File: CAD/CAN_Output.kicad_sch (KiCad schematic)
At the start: 10 parts, among them U4 MCP251863T-E/9PX, Y2 Crystal_GND24

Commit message: updated baord
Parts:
- C18, C19: value 11.5p -> 18p
- Y2: value Crystal_GND24 -> 40MHz
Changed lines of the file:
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@@
 	(label "OSC1"
 		(at 45.72 146.05 0)
-		(fields_autoplaced yes)
 		(effects
 			(font
@@
 	(label "OSC1"
 		(at 78.74 85.09 0)
-		(fields_autoplaced yes)
 		(effects
 			(font
@@
 	(label "OSC2"
 		(at 60.96 146.05 0)
-		(fields_autoplaced yes)
 		(effects
 			(font
@@
 	(label "OSC2"
 		(at 78.74 82.55 0)
-		(fields_autoplaced yes)
 		(effects
 			(font
@@
 		(shape output)
 		(at 154.94 85.09 0)
-		(fields_autoplaced yes)
 		(effects
 			(font
@@
 		(shape output)
 		(at 158.75 107.95 0)
-		(fields_autoplaced yes)
 		(effects
 			(font
@@
 		(shape input)
 		(at 154.94 87.63 0)
-		(fields_autoplaced yes)
 		(effects
 			(font
@@
 		(shape output)
 		(at 154.94 92.71 0)
-		(fields_autoplaced yes)
 		(effects
 			(font
@@
 		(shape output)
 		(at 78.74 92.71 180)
-		(fields_autoplaced yes)
 		(effects
 			(font
@@
 		(shape output)
 		(at 154.94 90.17 0)
-		(fields_autoplaced yes)
 		(effects
 			(font
@@
 		(shape output)
 		(at 78.74 80.01 180)
-		(fields_autoplaced yes)
 		(effects
 			(font
@@
 		(shape output)
 		(at 170.18 105.41 0)
-		(fields_autoplaced yes)
 		(effects
 			(font
@@
 			)
 		)
-		(property "Value" "11.5p"
+		(property "Value" "18p"
 			(at 41.91 151.1299 0)
 			(effects
@@
 			)
 		)
-		(property "Value" "11.5p"
+		(property "Value" "18p"
 			(at 66.04 151.1299 0)
 			(effects
@@
 			)
 		)
-		(property "Value" "Crystal_GND24"
+		(property "Value" "40MHz"
 			(at 67.31 142.2714 0)
 			(effects
@@
 			)
 		)
-		(property "Datasheet" "~"
+		(property "Datasheet" "ABM8G-40.000MHZ-18-D2Y-T"
 			(at 55.88 146.05 0)
 			(effects

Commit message: updated board
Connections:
- net GND: now also U4.29 (EP)
- net nINT1: now also U4.9 (nINT0/GPIO0/XSTBY); no longer U4.8 (nINT1/GPIO1)
- no-connect marks 4 -> 3
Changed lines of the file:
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@@
 	)
 	(no_connect
-		(at 154.94 74.93)
-	)
-	(no_connect
-		(at 83.82 95.25)
+		(at 83.82 92.71)
 	)
 	(no_connect
@@
 	(wire
 		(pts
+			(xy 154.94 74.93) (xy 166.37 74.93)
+		)
+		(stroke
+			(width 0)
+			(type default)
+		)
+	)
+	(wire
+		(pts
 			(xy 82.55 97.79) (xy 82.55 90.17)
 		)
@@
 	(wire
 		(pts
+			(xy 80.01 92.71) (xy 78.74 92.71)
+		)
+		(stroke
+			(width 0)
+			(type default)
+		)
+	)
+	(wire
+		(pts
 			(xy 83.82 97.79) (xy 82.55 97.79)
 		)
@@
 	(wire
 		(pts
-			(xy 78.74 92.71) (xy 83.82 92.71)
-		)
-		(stroke
-			(width 0)
-			(type default)
-		)
-	)
-	(wire
-		(pts
 			(xy 161.29 97.79) (xy 161.29 77.47)
 		)
@@
 	(wire
 		(pts
+			(xy 83.82 95.25) (xy 80.01 95.25)
+		)
+		(stroke
+			(width 0)
+			(type default)
+		)
+	)
+	(wire
+		(pts
 			(xy 78.74 85.09) (xy 83.82 85.09)
 		)
@@
 		(pts
 			(xy 71.12 115.57) (xy 82.55 115.57)
+		)
+		(stroke
+			(width 0)
+			(type default)
+		)
+	)
+	(wire
+		(pts
+			(xy 80.01 95.25) (xy 80.01 92.71)
 		)
 		(stroke
@@
 		)
 	)
+	(symbol
+		(lib_id "power:GND")
+		(at 166.37 74.93 0)
+		(unit 1)
+		(exclude_from_sim no)
+		(in_bom yes)
+		(on_board yes)
+		(dnp no)
+		(fields_autoplaced yes)
+		(property "Reference" "#PWR039"
+			(at 166.37 81.28 0)
+			(effects
+				(font
+					(size 1.27 1.27)
+				)
+				(hide yes)
+			)
+		)
+		(property "Value" "GND"
+			(at 166.37 80.01 0)
+			(effects
+				(font
+					(size 1.27 1.27)
+				)
+			)
+		)
+		(property "Footprint" ""
+			(at 166.37 74.93 0)
+			(effects
+				(font
+					(size 1.27 1.27)
+				)
+				(hide yes)
+			)
+		)
+		(property "Datasheet" ""
+			(at 166.37 74.93 0)
+			(effects
+				(font
+					(size 1.27 1.27)
+				)
+				(hide yes)
+			)
+		)
+		(property "Description" "Power symbol creates a global label with name \"GND\" , ground"
+			(at 166.37 74.93 0)
+			(effects
+				(font
+					(size 1.27 1.27)
+				)
+				(hide yes)
+			)
+		)
+		(pin "1"
+		)
+		(instances
+			(project ""
+				(path "/7d82ce85-7222-412b-9514-e26c0dea1256/32242d8d-0269-4405-8d3b-a17d7bfa44f1"
+					(reference "#PWR039")
+					(unit 1)
+				)
+				(path "/7d82ce85-7222-412b-9514-e26c0dea1256/3a8c1e9a-a729-42c6-9176-105dc8f8e86f"
+					(reference "#PWR071")
+					(unit 1)
+				)
+				(path "/7d82ce85-7222-412b-9514-e26c0dea1256/74c494bc-ee2a-4fe5-bc69-1ba1e57f619f"
+					(reference "#PWR056")
+					(unit 1)
+				)
+				(path "/7d82ce85-7222-412b-9514-e26c0dea1256/76451f76-fd73-4116-830f-890633fcbfa7"
+					(reference "#PWR073")
+					(unit 1)
+				)
+				(path "/7d82ce85-7222-412b-9514-e26c0dea1256/7c2b908d-9818-4bb6-93e9-a0140f4d4ed5"
+					(reference "#PWR074")
+					(unit 1)
+				)
+				(path "/7d82ce85-7222-412b-9514-e26c0dea1256/da33695d-32f0-4c7b-ab9e-83e6b0fd2dfd"
+					(reference "#PWR072")
+					(unit 1)
+				)
+			)
+		)
+	)

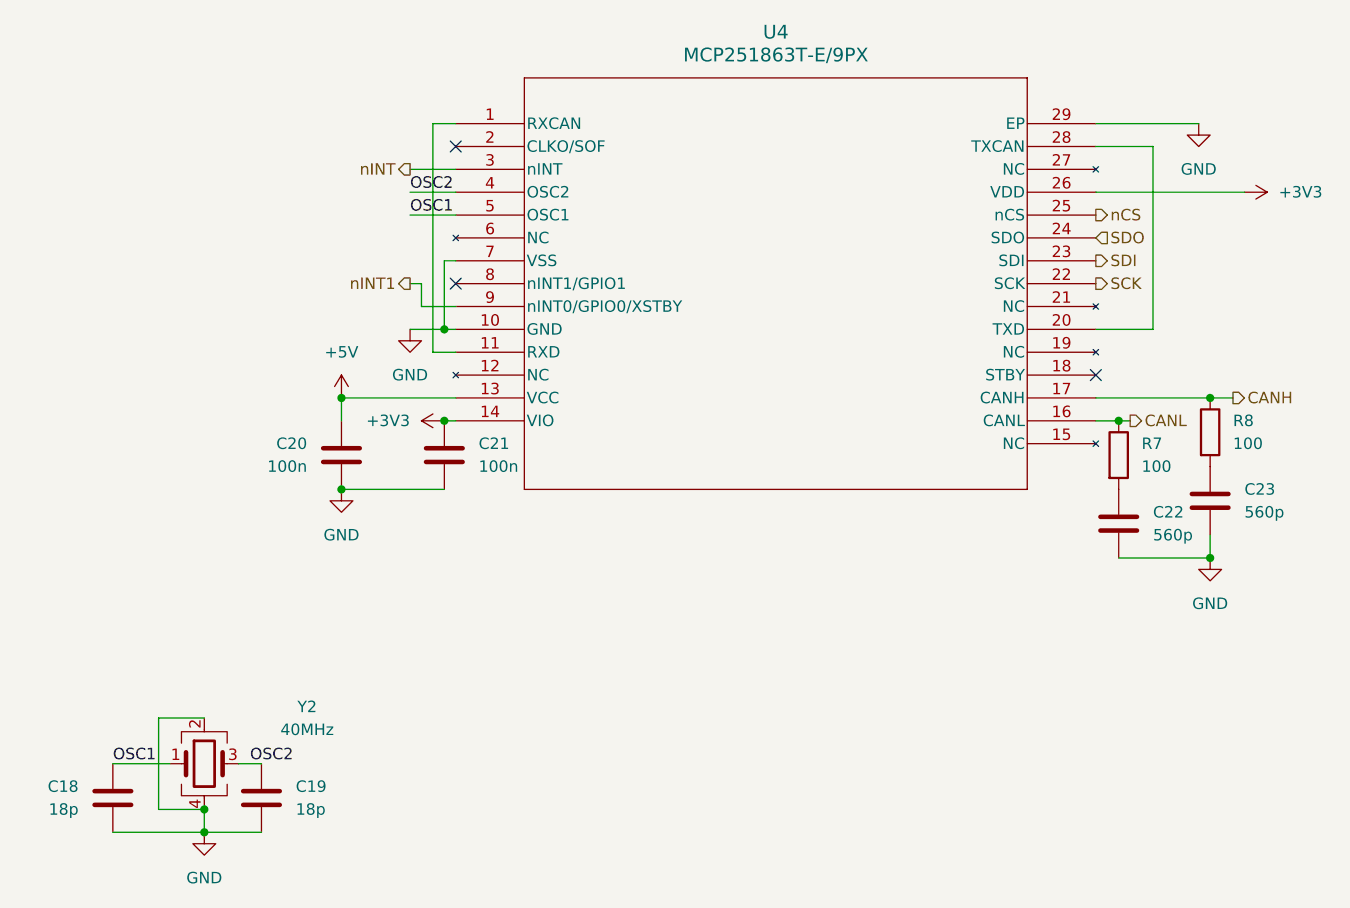
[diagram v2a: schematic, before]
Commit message: updated stby pinout
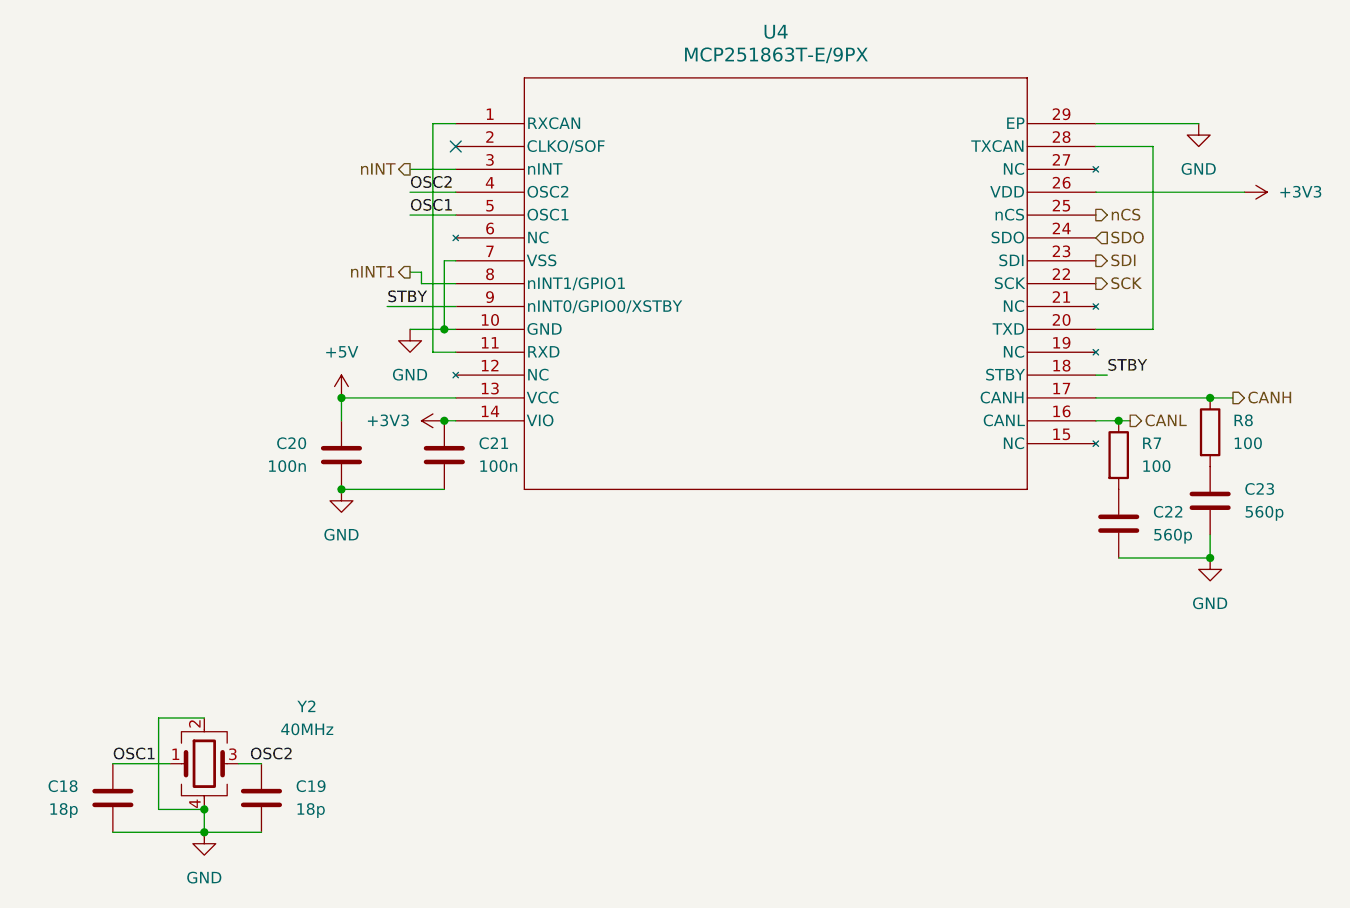
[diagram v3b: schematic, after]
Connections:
- net nINT1: now also U4.8 (nINT1/GPIO1); no longer U4.9 (nINT0/GPIO0/XSTBY)
- net STBY: now reaches U4.18 (STBY)
- net STBY: now also U4.9 (nINT0/GPIO0/XSTBY)
- no-connect marks 3 -> 1
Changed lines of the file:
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@@
-	)
-	(no_connect
-		(at 83.82 92.71)
-	)
-	(no_connect
-		(at 154.94 102.87)
 	)
 	(no_connect
@@
 	(wire
 		(pts
+			(xy 80.01 92.71) (xy 83.82 92.71)
+		)
+		(stroke
+			(width 0)
+			(type default)
+		)
+	)
+	(wire
+		(pts
 			(xy 82.55 107.95) (xy 83.82 107.95)
 		)
@@
 	(wire
 		(pts
-			(xy 80.01 92.71) (xy 78.74 92.71)
+			(xy 78.74 91.44) (xy 80.01 91.44)
 		)
 		(stroke
@@
 	(wire
 		(pts
+			(xy 76.2 95.25) (xy 83.82 95.25)
+		)
+		(stroke
+			(width 0)
+			(type default)
+		)
+	)
+	(wire
+		(pts
 			(xy 167.64 105.41) (xy 154.94 105.41)
 		)
@@
 	(wire
 		(pts
-			(xy 83.82 95.25) (xy 80.01 95.25)
-		)
-		(stroke
-			(width 0)
-			(type default)
-		)
-	)
-	(wire
-		(pts
 			(xy 78.74 85.09) (xy 83.82 85.09)
 		)
@@
 	(wire
 		(pts
-			(xy 80.01 95.25) (xy 80.01 92.71)
-		)
-		(stroke
-			(width 0)
-			(type default)
-		)
-	)
-	(wire
-		(pts
 			(xy 81.28 74.93) (xy 83.82 74.93)
 		)
@@
 	(wire
 		(pts
+			(xy 80.01 91.44) (xy 80.01 92.71)
+		)
+		(stroke
+			(width 0)
+			(type default)
+		)
+	)
+	(wire
+		(pts
+			(xy 156.21 102.87) (xy 154.94 102.87)
+		)
+		(stroke
+			(width 0)
+			(type default)
+		)
+	)
+	(wire
+		(pts
 			(xy 161.29 77.47) (xy 154.94 77.47)
 		)
@@
 			(width 0)
 			(type default)
+		)
+	)
+	(label "STBY"
+		(at 156.21 102.87 0)
+		(effects
+			(font
+				(size 1.27 1.27)
+			)
+			(justify left bottom)
 		)
 	)
@@
 	(label "OSC2"
 		(at 60.96 146.05 0)
+		(effects
+			(font
+				(size 1.27 1.27)
+			)
+			(justify left bottom)
+		)
+	)
+	(label "STBY"
+		(at 76.2 95.25 0)
 		(effects
 			(font
@@
 	(hierarchical_label "nINT1"
 		(shape output)
-		(at 78.74 92.71 180)
-		(effects
-			(font
+		(at 78.74 91.44 180)
+		(effects
+			(font

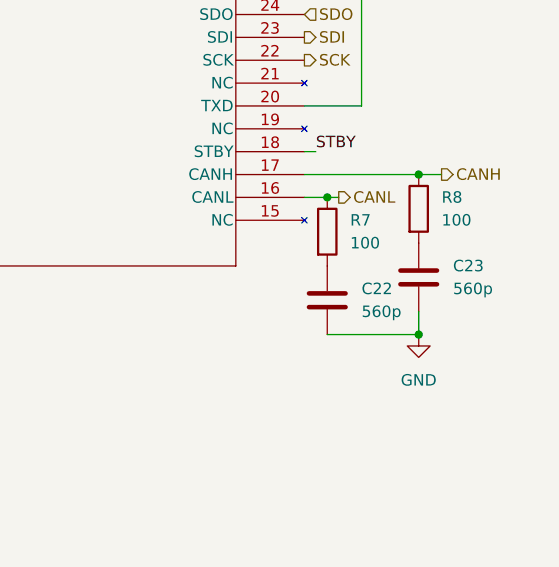
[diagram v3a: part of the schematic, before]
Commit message: updated CAN termination
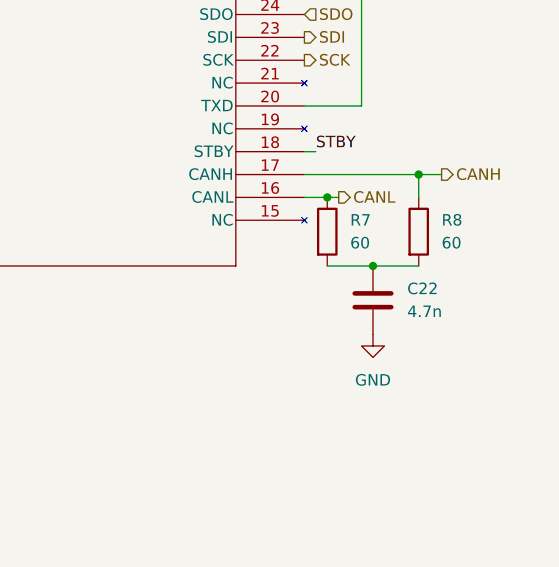
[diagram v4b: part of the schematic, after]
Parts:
- removed C23: 560p, Capacitor_SMD:C_0603_1608Metric, symbol Device:C
- C22: value 560p -> 4.7n
- R7, R8: value 100 -> 60
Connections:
- net at R8.2: now also C22.1, R7.2
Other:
- moved on the sheet: C22, R8
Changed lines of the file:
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@@
-	)
-	(junction
-		(at 167.64 123.19)
-		(diameter 0)
-		(color 0 0 0 0)
 	)
 	(junction
@@
 		(color 0 0 0 0)
 	)
+	(junction
+		(at 162.56 115.57)
+		(diameter 0)
+		(color 0 0 0 0)
+	)
 	(no_connect
 		(at 83.82 77.47)
@@
 	(wire
 		(pts
-			(xy 167.64 123.19) (xy 167.64 120.65)
-		)
-		(stroke
-			(width 0)
-			(type default)
-		)
-	)
-	(wire
-		(pts
 			(xy 154.94 74.93) (xy 166.37 74.93)
 		)
@@
 	(wire
 		(pts
+			(xy 162.56 115.57) (xy 167.64 115.57)
+		)
+		(stroke
+			(width 0)
+			(type default)
+		)
+	)
+	(wire
+		(pts
 			(xy 82.55 97.79) (xy 82.55 90.17)
 		)
@@
 	(wire
 		(pts
-			(xy 157.48 123.19) (xy 167.64 123.19)
-		)
-		(stroke
-			(width 0)
-			(type default)
-		)
-	)
-	(wire
-		(pts
 			(xy 83.82 100.33) (xy 81.28 100.33)
 		)
@@
 	(wire
 		(pts
+			(xy 167.64 107.95) (xy 167.64 105.41)
+		)
+		(stroke
+			(width 0)
+			(type default)
+		)
+	)
+	(wire
+		(pts
 			(xy 55.88 153.67) (xy 62.23 153.67)
 		)
@@
 		(pts
 			(xy 50.8 140.97) (xy 50.8 151.13)
+		)
+		(stroke
+			(width 0)
+			(type default)
+		)
+	)
+	(wire
+		(pts
+			(xy 162.56 115.57) (xy 157.48 115.57)
 		)
 		(stroke
@@
 				(path "/7d82ce85-7222-412b-9514-e26c0dea1256/da33695d-32f0-4c7b-ab9e-83e6b0fd2dfd"
 					(reference "#PWR072")
-					(unit 1)
-				)
-			)
-		)
-	)
-	(symbol
-		(lib_id "Device:C")
-		(at 167.64 116.84 0)
-		(unit 1)
-		(exclude_from_sim no)
-		(in_bom yes)
-		(on_board yes)
-		(dnp no)
-		(fields_autoplaced yes)
-		(property "Reference" "C23"
-			(at 171.45 115.5699 0)
-			(effects
-				(font
-					(size 1.27 1.27)
-				)
-				(justify left)
-			)
-		)
-		(property "Value" "560p"
-			(at 171.45 118.1099 0)
-			(effects
-				(font
-					(size 1.27 1.27)
-				)
-				(justify left)
-			)
-		)
-		(property "Footprint" "Capacitor_SMD:C_0603_1608Metric"
-			(at 168.6052 120.65 0)
-			(effects
-				(font
-					(size 1.27 1.27)
-				)
-				(hide yes)
-			)
-		)
-		(property "Datasheet" "~"
-			(at 167.64 116.84 0)
-			(effects
-				(font
-					(size 1.27 1.27)
-				)
-				(hide yes)
-			)
-		)
-		(property "Description" "Unpolarized capacitor"
-			(at 167.64 116.84 0)
-			(effects
-				(font
-					(size 1.27 1.27)
-				)
-				(hide yes)
-			)
-		)
-		(pin "2"
-		)
-		(pin "1"
-		)
-		(instances
-			(project "CAN Board"
-				(path "/7d82ce85-7222-412b-9514-e26c0dea1256/32242d8d-0269-4405-8d3b-a17d7bfa44f1"
-					(reference "C23")
-					(unit 1)
-				)
-				(path "/7d82ce85-7222-412b-9514-e26c0dea1256/3a8c1e9a-a729-42c6-9176-105dc8f8e86f"
-					(reference "C37")
-					(unit 1)
-				)
-				(path "/7d82ce85-7222-412b-9514-e26c0dea1256/74c494bc-ee2a-4fe5-bc69-1ba1e57f619f"
-					(reference "C30")
-					(unit 1)
-				)
-				(path "/7d82ce85-7222-412b-9514-e26c0dea1256/76451f76-fd73-4116-830f-890633fcbfa7"
-					(reference "C51")
-					(unit 1)
-				)
-				(path "/7d82ce85-7222-412b-9514-e26c0dea1256/7c2b908d-9818-4bb6-93e9-a0140f4d4ed5"
-					(reference "C58")
-					(unit 1)
-				)
-				(path "/7d82ce85-7222-412b-9514-e26c0dea1256/da33695d-32f0-4c7b-ab9e-83e6b0fd2dfd"
-					(reference "C44")
 					(unit 1)
 				)
@@
 	(symbol
 		(lib_id "Device:R")
-		(at 167.64 109.22 0)
+		(at 167.64 111.76 0)
 		(unit 1)
 		(exclude_from_sim no)
@@
 		(fields_autoplaced yes)
 		(property "Reference" "R8"
-			(at 170.18 107.9499 0)
+			(at 170.18 110.4899 0)
 			(effects
 				(font
@@
 			)
 		)
-		(property "Value" "100"
-			(at 170.18 110.4899 0)
+		(property "Value" "60"
+			(at 170.18 113.0299 0)
 			(effects
 				(font
@@
 		)
 		(property "Footprint" "Resistor_SMD:R_0603_1608Metric"
-			(at 165.862 109.22 90)
+			(at 165.862 111.76 90)
 			(effects
 				(font
@@
 		)
 		(property "Datasheet" "~"
-			(at 167.64 109.22 0)
+			(at 167.64 111.76 0)
 			(effects
 				(font
@@
 		)
 		(property "Description" "Resistor"
-			(at 167.64 109.22 0)
+			(at 167.64 111.76 0)
 			(effects
 				(font
@@
 			)
 		)
-		(property "Value" "100"
+		(property "Value" "60"
 			(at 160.02 113.0299 0)
 			(effects
@@
 	(symbol
 		(lib_id "power:GND")
-		(at 167.64 123.19 0)
+		(at 162.56 123.19 0)
 		(unit 1)
 		(exclude_from_sim no)
@@
 		(fields_autoplaced yes)
 		(property "Reference" "#PWR028"
-			(at 167.64 129.54 0)
+			(at 162.56 129.54 0)
 			(effects
 				(font
@@
 		)
 		(property "Value" "GND"
-			(at 167.64 128.27 0)
+			(at 162.56 128.27 0)
 			(effects
 				(font
@@
 		)
 		(property "Footprint" ""
-			(at 167.64 123.19 0)
+			(at 162.56 123.19 0)
 			(effects
 				(font
@@
 		)
 		(property "Datasheet" ""
-			(at 167.64 123.19 0)
+			(at 162.56 123.19 0)
 			(effects
 				(font
@@
 		)
 		(property "Description" "Power symbol creates a global label with name \"GND\" , ground"
-			(at 167.64 123.19 0)
+			(at 162.56 123.19 0)
 			(effects
 				(font
@@
 	(symbol
 		(lib_id "Device:C")
-		(at 157.48 119.38 0)
+		(at 162.56 119.38 0)
 		(unit 1)
 		(exclude_from_sim no)
@@
 		(fields_autoplaced yes)
 		(property "Reference" "C22"
-			(at 161.29 118.1099 0)
+			(at 166.37 118.1099 0)
 			(effects
 				(font
@@
 			)
 		)
-		(property "Value" "560p"
-			(at 161.29 120.6499 0)
+		(property "Value" "4.7n"
+			(at 166.37 120.6499 0)
 			(effects
 				(font
@@
 		)
 		(property "Footprint" "Capacitor_SMD:C_0603_1608Metric"
-			(at 158.4452 123.19 0)
+			(at 163.5252 123.19 0)
 			(effects
 				(font
@@
 		)
 		(property "Datasheet" "~"
-			(at 157.48 119.38 0)
+			(at 162.56 119.38 0)
 			(effects
 				(font
@@
 		)
 		(property "Description" "Unpolarized capacitor"
-			(at 157.48 119.38 0)
-			(effects
-				(font
+			(at 162.56 119.38 0)
+			(effects
+				(font
